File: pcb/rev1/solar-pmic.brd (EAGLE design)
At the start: 21 x 32 mm, 82 parts, among them IC2 MCP6002, IC3 MCP6002, IC4 LM3671MF-ADJ, IC5 TS520525, IC6 STM32F030X4, Q1 BSS123

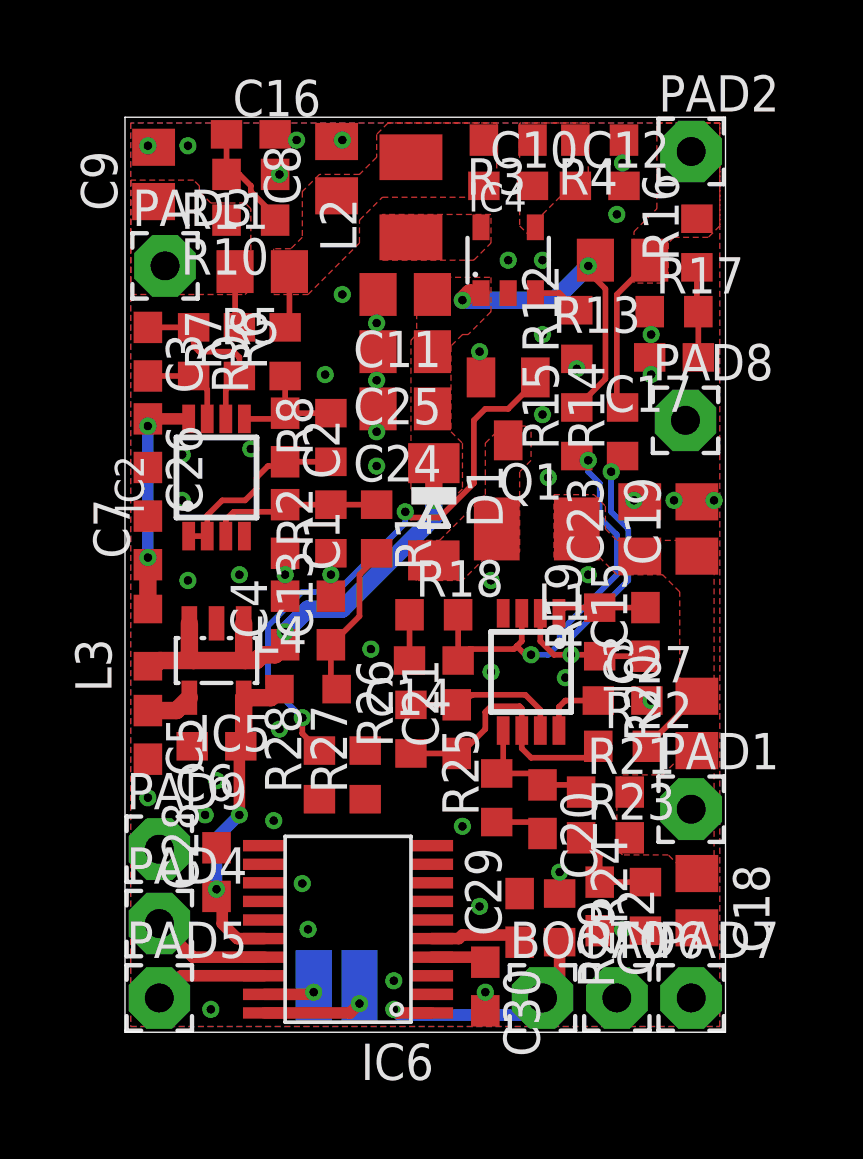
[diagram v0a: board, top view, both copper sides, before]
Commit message: Minor schematic fixes + final routing + annotation.
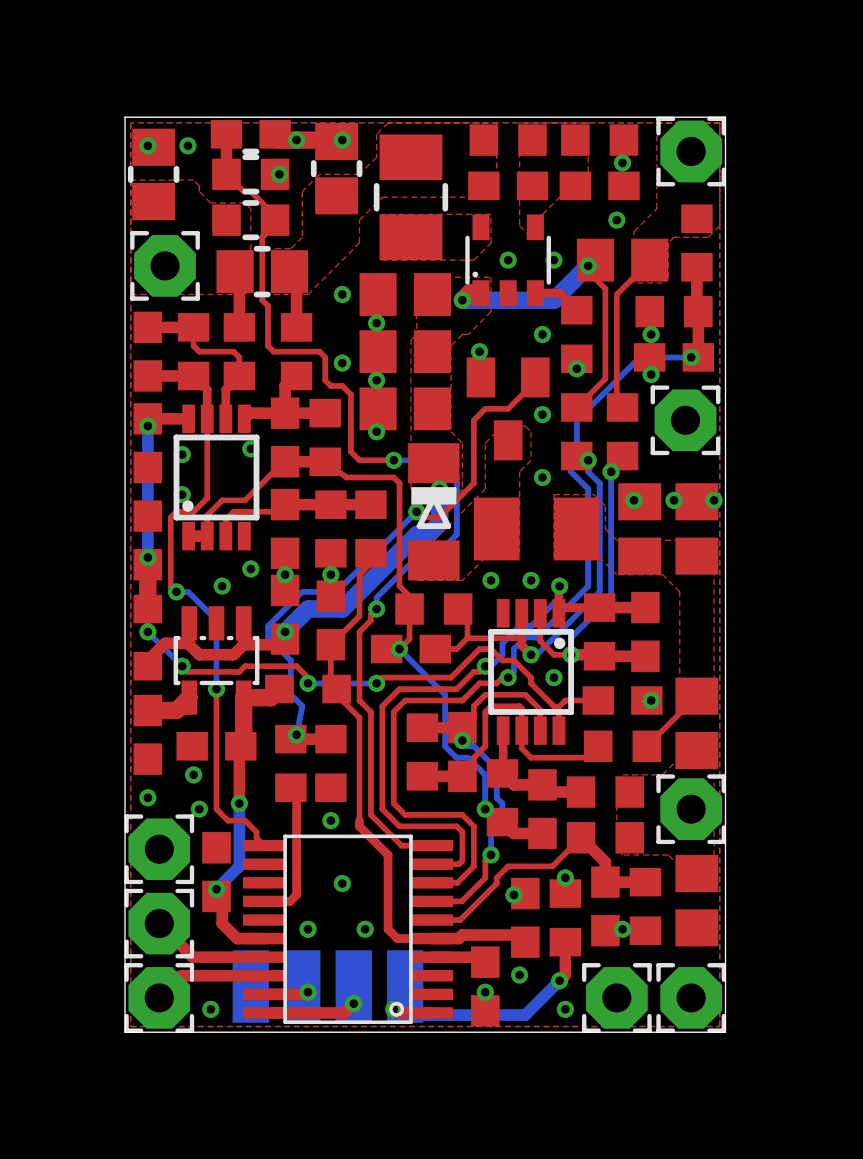
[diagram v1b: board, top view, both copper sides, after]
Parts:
- added SWGND: (no value), wirepad:SMD1,27-2,54
- BOOT0: device wirepad:2,15/1,0 -> wirepad:SMD1,27-2,54
- moved BOOT0 4.82 mm to (22.2, 6.80), flipped to the bottom
- moved R27 2.63 mm to (18.2, 14.6)
- moved C14 0.89 mm to (22.4, 18.6)
- moved R26 0.89 mm to (22.8, 15.0)
- moved C21 0.82 mm to (24.2, 15.0)
- moved R28 0.57 mm to (19.6, 14.6)
- moved R6 0.40 mm to (18.4, 29.0)
- moved SWDIO 0.40 mm to (18.6, 6.80)
- moved R25 0.20 mm to (25.6, 13.4)
- moved R8 0.20 mm to (19.4, 26.0)
- moved SWCLK 0.20 mm to (20.4, 6.80)
- moved C22 0.20 mm to (29.2, 9.60)
- moved C29 0.20 mm to (26.4, 9.20)
- moved C4 0.20 mm to (18.0, 19.8)
- moved R1 0.20 mm to (21.0, 22.8)
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- renumbered PAD1 to SOLAR, PAD2 to VBAT, PAD3 to VOUT, PAD4 to SCL, PAD5 to SDA, PAD6 to G1, PAD7 to G2, PAD8 to G3, PAD9 to G4
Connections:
- net GND: now also SWGND.1
- net VDDO_ENA: now also IC6.13
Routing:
- net VDDO_USENSE: track 3.97 -> 35.0 mm, vias 0 -> 2
- net VBATO_USENSE: track 3.17 -> 33.0 mm, vias 0 -> 2
- net VBATO_ISENSE: track 3.11 -> 21.3 mm, vias 0 -> 2
- net VDDO_ISENSE: track 3.30 -> 21.0 mm, vias 0 -> 2
- net VDDA4: track 10.4 -> 28.0 mm, vias 2 -> 6
- net VDDA2: track 10.1 -> 25.1 mm, vias 0 -> 2
- net VDDA: track 8.73 -> 19.8 mm
- net SOLARO_ISENSE: track 5.57 -> 14.2 mm, vias 0 -> 2
- net SOLARO_USENSE: track 3.42 -> 9.84 mm
- net GATE: track 0.00 -> 5.05 mm
- net GND: track 0.00 -> 3.52 mm, vias 52 -> 49
- net VBAT: track 28.7 -> 27.3 mm
- net N$15: track 9.06 -> 10.2 mm, vias 1 -> 2
- net N$4: track 19.8 -> 20.5 mm
- net N$14: track 15.0 -> 14.5 mm
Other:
- board text added: "solar-pmm rev1 (20141202) (c) qyx@krtko.org, CC-BY-SA"

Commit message: Layout changes.
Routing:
- net VDDO_ENA: track 1.70 -> 35.7 mm, vias 0 -> 2
- net VBAT: track 27.3 -> 27.9 mm
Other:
- board text added: "MCU + vreg"
- board text added: "current & voltage sensing"
- board text added: "solar charger"
- board text added: "vout power supply"
